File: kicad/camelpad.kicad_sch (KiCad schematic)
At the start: 29 parts, among them J1 USB_C_Receptacle_USB2.0_16P, J2 USB_C_Receptacle_USB2.0_16P, J3 AVR-UPDI, SW1 SWITCH_PUSHBUTTON_KAILH_SOCKET, SW2 SWITCH_PUSHBUTTON_KAILH_SOCKET, SW3 SWITCH_PUSHBUTTON_KAILH_SOCKET, SW4 SWITCH_PUSHBUTTON_KAILH_SOCKET, SW5 SWITCH_PUSHBUTTON_KAILH_SOCKET, SW6 SWITCH_PUSHBUTTON_KAILH_SOCKET, U1 ATtiny816-M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

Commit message: Schematic Cleanup
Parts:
- added R1: 3K3, camelpad:R_0402_1005Metric, symbol Device:R
- I2C1: renamed from CONN1; value ~ -> I2C; symbol camelpad:STEMMA_I2C_QTRA -> camelpad:STEMMA_I2C_JST_SH_4P
- UPDI1: renamed from J3; footprint camelpad:JST_SH_BM04B-SRSS-TB_1x03-1MP_P1.00mm_Vertical -> camelpad:JST_SH_BM04B-SRSS-TB_1x04-1MP_P1.00mm_Vertical; symbol camelpad:UPDI_JST_SH_3P -> camelpad:UPDI_JST_SH_4P
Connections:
- net GND: now also UPDI1.1 (GND), UPDI1.5 (MP), UPDI1.6 (MP); no longer UPDI1.3 (GND), UPDI1.MP
- net UPDI: now also UPDI1.4 (RX), R1.2; no longer UPDI1.1 (UPDI)
- net VCC: no longer UPDI1.2 (V+)
- net VIN: now also UPDI1.2 (V+)
- new net: R1.1, UPDI1.3 (TX)
- no-connect marks 0 -> 8
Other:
- moved on the sheet: D1, D2, D3, SW1, SW2, SW3

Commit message: Update KiCad project
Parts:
- D1, D2, D3, D4, D5, D6: footprint Diode_SMD:D_SOD-323 -> camelpad:D_SOD-323; symbol Diode:1N4148WS -> camelpad:1N4148
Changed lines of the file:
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@@
 	)
 	(symbol
-		(lib_id "Diode:1N4148WS")
+		(lib_id "camelpad:1N4148")
 		(at 214.63 36.83 180)
 		(unit 1)
@@
 			)
 		)
-		(property "Footprint" "Diode_SMD:D_SOD-323"
-			(at 214.63 32.385 0)
-			(effects
-				(font
-					(size 1.27 1.27)
-				)
-				(hide yes)
-			)
-		)
-		(property "Datasheet" "https://www.vishay.com/docs/85751/1n4148ws.pdf"
+		(property "Footprint" "camelpad:D_SOD-323"
 			(at 214.63 36.83 0)
 			(effects
@@
 			)
 		)
-		(property "Description" "75V 0.15A Fast switching Diode, SOD-323"
+		(property "Datasheet" "https://assets.nexperia.com/documents/data-sheet/1N4148_1N4448.pdf"
+			(at 214.63 36.83 0)
+			(effects
+				(font
+					(size 1.27 1.27)
+				)
+				(hide yes)
+			)
+		)
+		(property "Description" "100V 0.15A standard switching diode, DO-35"
 			(at 214.63 36.83 0)
 			(effects
@@
 	)
 	(symbol
-		(lib_id "Diode:1N4148WS")
+		(lib_id "camelpad:1N4148")
 		(at 214.63 48.26 180)
 		(unit 1)
@@
 			)
 		)
-		(property "Footprint" "Diode_SMD:D_SOD-323"
-			(at 214.63 43.815 0)
-			(effects
-				(font
-					(size 1.27 1.27)
-				)
-				(hide yes)
-			)
-		)
-		(property "Datasheet" "https://www.vishay.com/docs/85751/1n4148ws.pdf"
+		(property "Footprint" "camelpad:D_SOD-323"
 			(at 214.63 48.26 0)
 			(effects
@@
 			)
 		)
-		(property "Description" "75V 0.15A Fast switching Diode, SOD-323"
+		(property "Datasheet" "https://assets.nexperia.com/documents/data-sheet/1N4148_1N4448.pdf"
+			(at 214.63 48.26 0)
+			(effects
+				(font
+					(size 1.27 1.27)
+				)
+				(hide yes)
+			)
+		)
+		(property "Description" "100V 0.15A standard switching diode, DO-35"
 			(at 214.63 48.26 0)
 			(effects
@@
 	)
 	(symbol
-		(lib_id "Diode:1N4148WS")
+		(lib_id "camelpad:1N4148")
 		(at 214.63 25.4 180)
 		(unit 1)
@@
 			)
 		)
-		(property "Footprint" "Diode_SMD:D_SOD-323"
-			(at 214.63 20.955 0)
-			(effects
-				(font
-					(size 1.27 1.27)
-				)
-				(hide yes)
-			)
-		)
-		(property "Datasheet" "https://www.vishay.com/docs/85751/1n4148ws.pdf"
+		(property "Footprint" "camelpad:D_SOD-323"
 			(at 214.63 25.4 0)
 			(effects
@@
 			)
 		)
-		(property "Description" "75V 0.15A Fast switching Diode, SOD-323"
+		(property "Datasheet" "https://assets.nexperia.com/documents/data-sheet/1N4148_1N4448.pdf"
+			(at 214.63 25.4 0)
+			(effects
+				(font
+					(size 1.27 1.27)
+				)
+				(hide yes)
+			)
+		)
+		(property "Description" "100V 0.15A standard switching diode, DO-35"
 			(at 214.63 25.4 0)
 			(effects
@@
 	)
 	(symbol
-		(lib_id "Diode:1N4148WS")
+		(lib_id "camelpad:1N4148")
 		(at 254 36.83 180)
 		(unit 1)
@@
 			)
 		)
-		(property "Footprint" "Diode_SMD:D_SOD-323"
-			(at 254 32.385 0)
-			(effects
-				(font
-					(size 1.27 1.27)
-				)
-				(hide yes)
-			)
-		)
-		(property "Datasheet" "https://www.vishay.com/docs/85751/1n4148ws.pdf"
+		(property "Footprint" "camelpad:D_SOD-323"
 			(at 254 36.83 0)
 			(effects
@@
 			)
 		)
-		(property "Description" "75V 0.15A Fast switching Diode, SOD-323"
+		(property "Datasheet" "https://assets.nexperia.com/documents/data-sheet/1N4148_1N4448.pdf"
+			(at 254 36.83 0)
+			(effects
+				(font
+					(size 1.27 1.27)
+				)
+				(hide yes)
+			)
+		)
+		(property "Description" "100V 0.15A standard switching diode, DO-35"
 			(at 254 36.83 0)
 			(effects
@@
 	)
 	(symbol
-		(lib_id "Diode:1N4148WS")
+		(lib_id "camelpad:1N4148")
 		(at 254 48.26 180)
 		(unit 1)
@@
 			)
 		)
-		(property "Footprint" "Diode_SMD:D_SOD-323"
-			(at 254 43.815 0)
-			(effects
-				(font
-					(size 1.27 1.27)
-				)
-				(hide yes)
-			)
-		)
-		(property "Datasheet" "https://www.vishay.com/docs/85751/1n4148ws.pdf"
+		(property "Footprint" "camelpad:D_SOD-323"
 			(at 254 48.26 0)
 			(effects
@@
 			)
 		)
-		(property "Description" "75V 0.15A Fast switching Diode, SOD-323"
+		(property "Datasheet" "https://assets.nexperia.com/documents/data-sheet/1N4148_1N4448.pdf"
+			(at 254 48.26 0)
+			(effects
+				(font
+					(size 1.27 1.27)
+				)
+				(hide yes)
+			)
+		)
+		(property "Description" "100V 0.15A standard switching diode, DO-35"
 			(at 254 48.26 0)
 			(effects
@@
 	)
 	(symbol
-		(lib_id "Diode:1N4148WS")
+		(lib_id "camelpad:1N4148")
 		(at 254 25.4 180)
 		(unit 1)
@@
 			)
 		)
-		(property "Footprint" "Diode_SMD:D_SOD-323"
-			(at 254 20.955 0)
-			(effects
-				(font
-					(size 1.27 1.27)
-				)
-				(hide yes)
-			)
-		)
-		(property "Datasheet" "https://www.vishay.com/docs/85751/1n4148ws.pdf"
+		(property "Footprint" "camelpad:D_SOD-323"
 			(at 254 25.4 0)
 			(effects
@@
 			)
 		)
-		(property "Description" "75V 0.15A Fast switching Diode, SOD-323"
+		(property "Datasheet" "https://assets.nexperia.com/documents/data-sheet/1N4148_1N4448.pdf"
 			(at 254 25.4 0)
 			(effects
+				(font
+					(size 1.27 1.27)
+				)
+				(hide yes)
+			)
+		)
+		(property "Description" "100V 0.15A standard switching diode, DO-35"
+			(at 254 25.4 0)
+			(effects

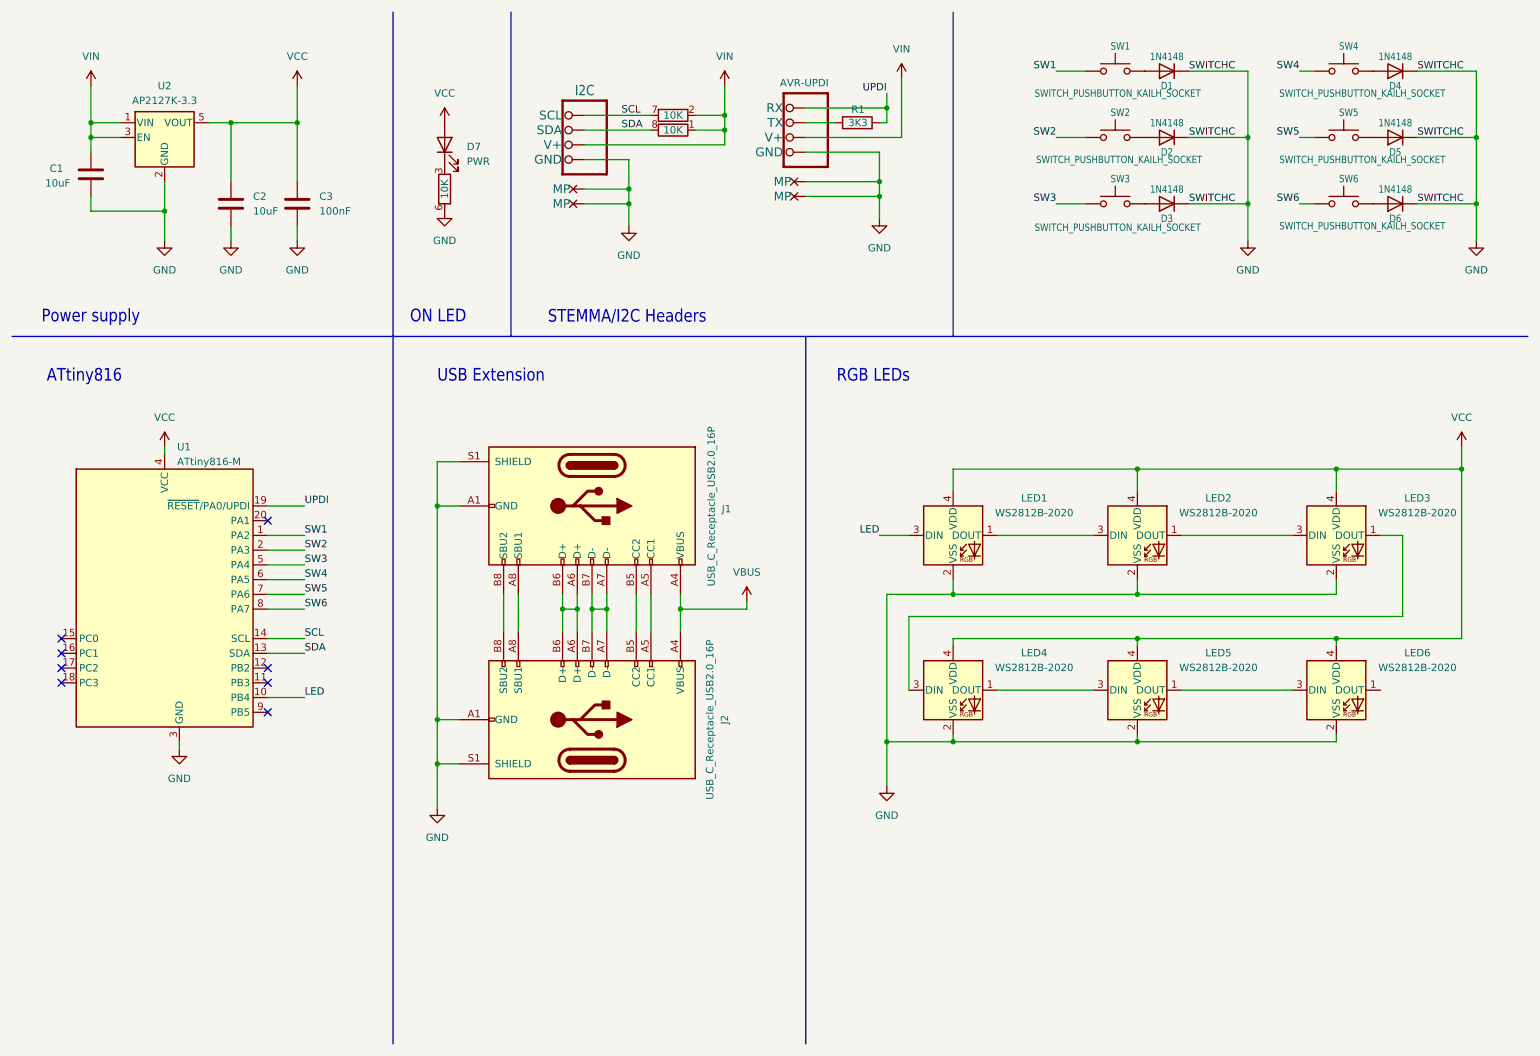
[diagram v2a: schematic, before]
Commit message: Update usb connector to molex picoblade
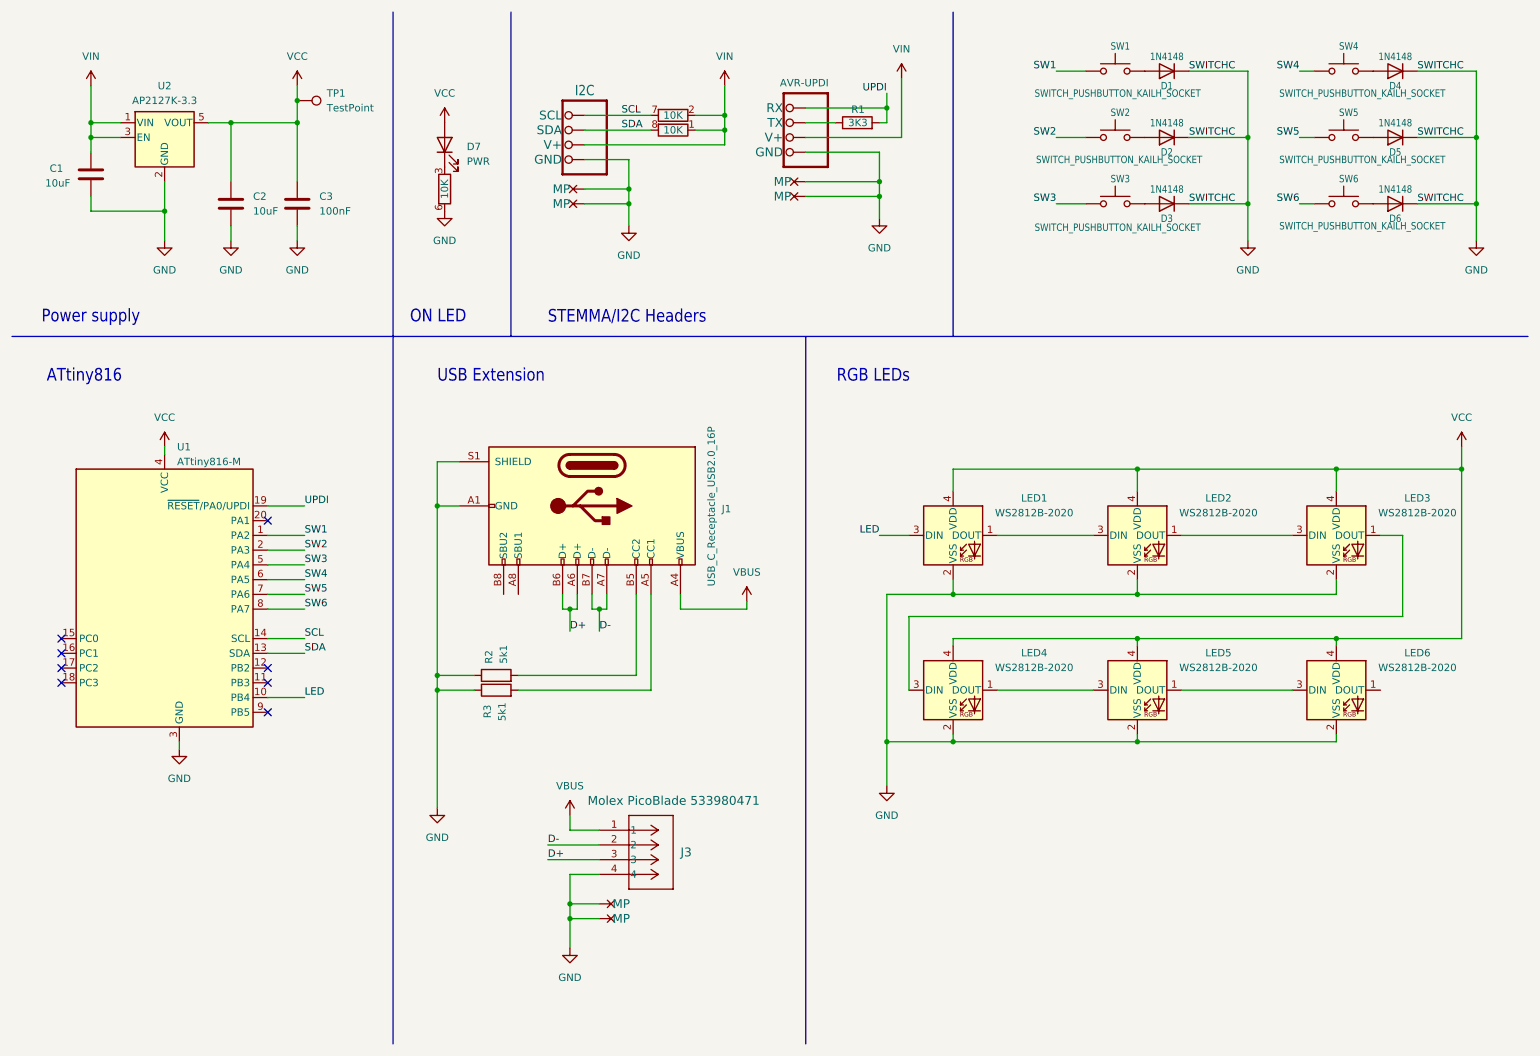
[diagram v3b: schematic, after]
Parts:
- removed J2: USB_C_Receptacle_USB2.0_16P, camelpad:USB-C-SMD_GT-USB-7055E, symbol camelpad:USB_C_Receptacle_USB2.0_16P
- added J3: Molex PicoBlade 533980471, CONN_53398_04_MOL, symbol camelpad:Molex_PicoBlade_4P_Vertical
- added R2, R3: 5k1, camelpad:R_0402_1005Metric, symbol Device:R
- added TP1: TestPoint, TestPoint:TestPoint_Pad_D1.0mm, symbol Connector:TestPoint
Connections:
- net GND: now also J3.4, J3.5 (MP), J3.6 (MP), R2.1, R3.1
- net VBUS: now also J3.1
- net VCC: now also TP1.1
- net at J1.A5 (CC1): now also R3.2
- net D+: now reaches J1.A6 (D+), J1.B6 (D+)
- net D+: now also J3.3
- net D-: now reaches J1.A7 (D-), J1.B7 (D-)
- net D-: now also J3.2
- net at J1.B5 (CC2): now also R2.2

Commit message: Update design rules and component footprints in camelpad project
- Added multiple DRC exclusions for silk and copper layers in camelpad.kicad_pro to improve layout integrity.
- Adjusted solder mask to copper clearance from 0.0 to 0.005 for better manufacturing tolerance.
- Updated component footprints in camelpad.kicad_sch from 0402 to 0603 for resistors and capacitors to accommodate new specifications.
- Changed LED footprint to a specific camelpad variant for improved compatibility.
- Modified resistor array footprints from 4x0603 to 4x1206 to reflect updated design requirements.
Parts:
- C1, C2, C3: footprint Capacitor_SMD:C_0603_1608Metric -> camelpad:C_0603_1608Metric
- D7: footprint LED_SMD:LED_0402_1005Metric -> camelpad:LED_0603_1608Metric_Pad1.05x0.95mm_HandSolder
- J3: footprint CONN_53398_04_MOL -> camelpad:CONN_53398_04_MOL
- R1, R2, R3: footprint camelpad:R_0402_1005Metric -> camelpad:R_0603_1608Metric
- RN1: footprint camelpad:R_Array_Convex_4x0603 -> camelpad:R_Array_Convex_4x1206
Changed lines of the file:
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@@
 			)
 		)
-		(property "Footprint" "camelpad:R_0402_1005Metric"
+		(property "Footprint" "camelpad:R_0603_1608Metric"
 			(at 99.06 133.858 90)
 			(effects
@@
 			)
 		)
-		(property "Footprint" "camelpad:R_0402_1005Metric"
+		(property "Footprint" "camelpad:R_0603_1608Metric"
 			(at 161.29 36.068 90)
 			(effects
@@
 			)
 		)
-		(property "Footprint" "camelpad:R_0402_1005Metric"
+		(property "Footprint" "camelpad:R_0603_1608Metric"
 			(at 99.06 131.318 90)
 			(effects
@@
 			)
 		)
-		(property "Footprint" "Capacitor_SMD:C_0603_1608Metric"
+		(property "Footprint" "camelpad:C_0603_1608Metric"
 			(at 54.3052 52.07 0)
 			(effects
@@
 			)
 		)
-		(property "Footprint" "LED_SMD:LED_0402_1005Metric"
+		(property "Footprint" "camelpad:LED_0603_1608Metric_Pad1.05x0.95mm_HandSolder"
 			(at 90.17 38.1 0)
 			(effects
@@
 			)
 		)
-		(property "Footprint" "Capacitor_SMD:C_0603_1608Metric"
+		(property "Footprint" "camelpad:C_0603_1608Metric"
 			(at 28.2448 39.37 0)
 			(effects
@@
 			)
 		)
-		(property "Footprint" "CONN_53398_04_MOL"
+		(property "Footprint" "camelpad:CONN_53398_04_MOL"
 			(at 121.666 168.402 0)
 			(effects
@@
 			)
 		)
-		(property "Footprint" "Capacitor_SMD:C_0603_1608Metric"
+		(property "Footprint" "camelpad:C_0603_1608Metric"
 			(at 65.7352 52.07 0)
 			(effects
@@
 			)
 		)
-		(property "Footprint" "camelpad:R_Array_Convex_4x0603"
+		(property "Footprint" "camelpad:R_Array_Convex_4x1206"
 			(at 92.202 45.72 90)
 			(effects
@@
 			)
 		)
-		(property "Footprint" "camelpad:R_Array_Convex_4x0603"
+		(property "Footprint" "camelpad:R_Array_Convex_4x1206"
 			(at 129.54 35.052 90)
 			(effects
@@
 			)
 		)
-		(property "Footprint" "camelpad:R_Array_Convex_4x0603"
+		(property "Footprint" "camelpad:R_Array_Convex_4x1206"
 			(at 129.54 37.592 90)
 			(effects
